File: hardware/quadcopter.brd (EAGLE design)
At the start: 132 x 132 mm, 69 parts, among them J2 AVR_SPI_PRG_6-SMD, J3 HEADER-10POSTH-254X10, J4 HEADER-4POS-0.1IN-FEMALE-SMD-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, J6 HEADER-4POS-0.1IN-FEMALE, Q3 MOSFET-FET-SI2302CDS-T1-E3CT-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, Q4 MOSFET-FET-SI2302CDS-T1-E3CT-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, Q5 MOSFET-FET-SI2302CDS-T1-E3CT-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, Q6 MOSFET-FET-SI2302CDS-T1-E3CT-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, U1 ATMEGA128RFA1, U2 IMU-LSM6DSOXTR-497-18367-1-ND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

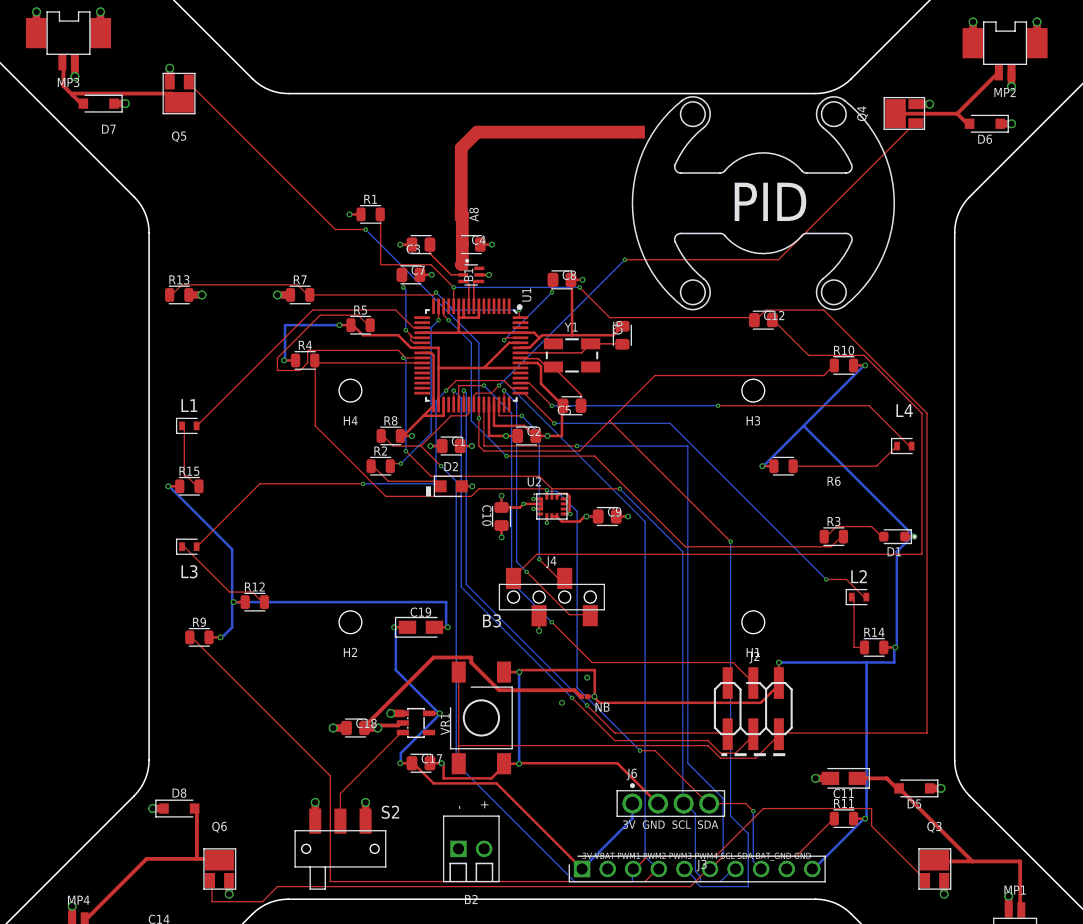
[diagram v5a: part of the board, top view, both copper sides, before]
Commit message: fixed high-current net issues
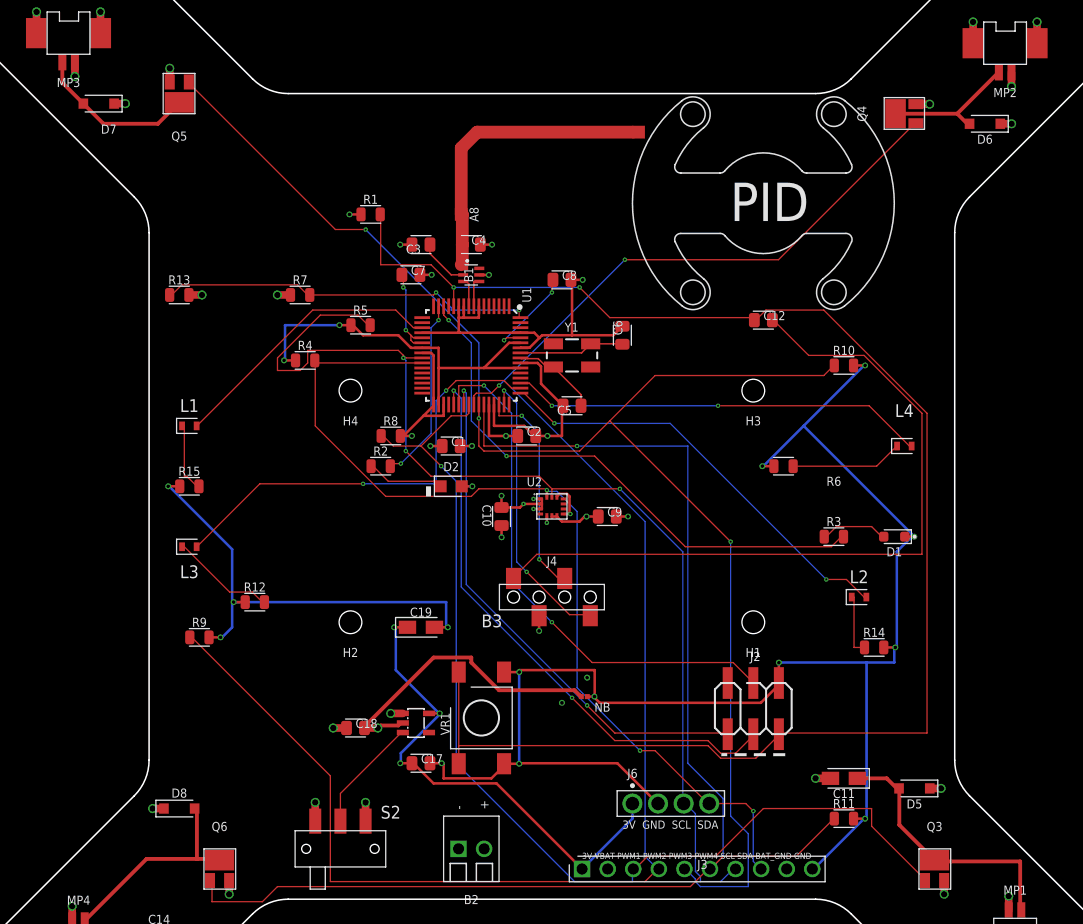
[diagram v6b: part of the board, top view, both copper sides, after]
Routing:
- net N$18: track 28.4 -> 26.7 mm
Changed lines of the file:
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@@
 <class number="1" name="HIGH-I" width="0.381" drill="0">
 </class>
-<class number="3" name="POWER" width="0" drill="0">
+<class number="3" name="PWR" width="0.254" drill="0">
 </class>
 <class number="4" name="RFSIG" width="0" drill="0">
@@
 </via>
 </signal>
-<signal name="N$18">
+<signal name="N$18" class="1">
 <contactref element="Q3" pad="D"/>
 <contactref element="MP1" pad="2"/>
@@
 <wire x1="34.25" y1="-28" x2="34.475" y2="-28" width="0.381" layer="1"/>
 <wire x1="46.5" y1="-35.25" x2="46.5" y2="-40" width="0.381" layer="1"/>
-<wire x1="38" y1="-35.25" x2="41.75" y2="-35.25" width="0.381" layer="1"/>
-<wire x1="41.75" y1="-35.25" x2="46.5" y2="-35.25" width="0.381" layer="1"/>
+<wire x1="38" y1="-35.25" x2="46.5" y2="-35.25" width="0.381" layer="1"/>
 <wire x1="46.5" y1="-40" x2="46.6125" y2="-40.1" width="0.381" layer="1"/>
 <wire x1="38" y1="-35.25" x2="38" y2="-35.125" width="0.381" layer="1"/>
-<wire x1="41.75" y1="-35.25" x2="34.5" y2="-28" width="0.381" layer="1"/>
 <wire x1="34.5" y1="-28" x2="34.475" y2="-28" width="0.381" layer="1"/>
-</signal>
-<signal name="N$19">
+<wire x1="38" y1="-35.125" x2="34.5" y2="-31.625" width="0.381" layer="1"/>
+<wire x1="34.5" y1="-31.625" x2="34.5" y2="-28" width="0.381" layer="1"/>
+</signal>
+<signal name="N$19" class="1">
 <contactref element="Q4" pad="D"/>
 <contactref element="MP2" pad="2"/>
@@
 <wire x1="44.25" y1="43" x2="44.3875" y2="43.1" width="0.381" layer="1"/>
 </signal>
-<signal name="N$20">
+<signal name="N$20" class="1">
 <contactref element="Q5" pad="D"/>
 <contactref element="MP3" pad="2"/>
 <contactref element="D7" pad="2"/>
-<wire x1="-48.5" y1="41.75" x2="-47.625" y2="40.875" width="0.381" layer="1"/>
-<wire x1="-47.625" y1="40.875" x2="-46.75" y2="40" width="0.381" layer="1"/>
-<wire x1="-48.5" y1="44" x2="-48.5" y2="41.75" width="0.381" layer="1"/>
-<wire x1="-46.75" y1="40" x2="-46.525" y2="40" width="0.381" layer="1"/>
-<wire x1="-48.5" y1="44" x2="-48.6125" y2="44.1" width="0.381" layer="1"/>
-<wire x1="-37.75" y1="41" x2="-37" y2="40.25" width="0.381" layer="1"/>
-<wire x1="-47.5" y1="41" x2="-37.75" y2="41" width="0.381" layer="1"/>
-<wire x1="-37" y1="40.25" x2="-37" y2="40.125" width="0.381" layer="1"/>
-<wire x1="-47.5" y1="41" x2="-47.625" y2="40.875" width="0.381" layer="1"/>
-</signal>
-<signal name="N$21">
+<wire x1="-48.6125" y1="44.1" x2="-48.6125" y2="42.0875" width="0.381" layer="1"/>
+<wire x1="-48.6125" y1="42.0875" x2="-46.525" y2="40" width="0.381" layer="1"/>
+<wire x1="-37" y1="40.125" x2="-39.125" y2="38" width="0.381" layer="1"/>
+<wire x1="-39.125" y1="38" x2="-44.525" y2="38" width="0.381" layer="1"/>
+<wire x1="-44.525" y1="38" x2="-46.525" y2="40" width="0.381" layer="1"/>
+</signal>
+<signal name="N$21" class="1">
 <contactref element="Q6" pad="D"/>
 <contactref element="MP4" pad="2"/>

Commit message: i really hope this passes
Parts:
- moved LOGO 58.8 mm to (12.0, -19.1)
- moved J6 26.6 mm to (-1.00, -4.50), turned to 0.9 degrees
- moved D7 25.5 mm to (-34.0, 17.0)
- moved MP3 21.2 mm to (-33.0, 32.0)
- moved C14 20.8 mm to (-27.0, -25.5)
- moved MP4 19.8 mm to (-33.0, -30.0)
- moved J2 19.3 mm to (19.9, -0.77)
- moved Q5 18.4 mm to (-33.0, 23.0)
- moved D6 18.0 mm to (28.0, 28.0), turned to 0 degrees
- moved MP1 17.8 mm to (35.0, -29.0)
- moved Q6 17.1 mm to (-27.0, -20.0)
- moved MP2 16.6 mm to (35.3, 32.5)
- moved Q3 16.1 mm to (36.0, -20.0)
- moved D5 14.0 mm to (36.0, -14.0)
- moved Q4 14.0 mm to (35.0, 25.0)
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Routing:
- net GND: track 291.8 -> 66.3 mm, vias 29 -> 28
- net SCL: track 108.5 -> 75.0 mm, vias 3 -> 2
- net N$13: track 74.3 -> 42.8 mm, vias 0 -> 2
- net PWM2: track 174.2 -> 146.1 mm, vias 2 -> 1
- net RESET: track 157.8 -> 133.8 mm, vias 2 -> 4
- net PWM4: track 135.8 -> 112.2 mm, vias 1 -> 2
- net MISO: track 52.8 -> 32.6 mm
- net MOSI: track 53.2 -> 36.1 mm
- net SCK: track 57.9 -> 43.3 mm
- net PWM3: track 149.4 -> 135.9 mm
- net SDA: track 94.5 -> 82.3 mm, vias 3 -> 2
- net BATMEASURE: track 37.4 -> 45.8 mm
- net PWM1: track 103.5 -> 96.1 mm
- net N$21: track 21.3 -> 14.8 mm
- net 3V: track 105.0 -> 98.9 mm, vias 12 -> 13
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- added copper zone on layer 1, net GND
- added copper zone on layer 16, net GND
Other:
- outline, holes or cut-outs redrawn

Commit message: i really hope this one passes
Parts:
- moved R4 17.7 mm to (-15.5, -0.70)
- moved C18 5.92 mm to (-14.6, -25.0)
- moved C19 5.74 mm to (-15.2, -17.3)
- moved C7 4.60 mm to (-18.6, 23.0)
- moved C3 2.94 mm to (-12.5, 23.1)
- moved C17 2.89 mm to (-16.0, -29.8)
- moved B3 1.66 mm to (-8.50, -21.0)
- moved C9 1.41 mm to (6.50, 0.00)
- moved R7 0.92 mm to (-25.7, 21.6)
- moved Q4 0.80 mm to (35.0, 24.2)
- moved C11 0.20 mm to (29.1, -20.0)
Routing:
- net PWM2: track 146.1 -> 159.9 mm, vias 1 -> 3
- net SCL: track 75.0 -> 85.4 mm, vias 2 -> 1
- net PWM3: track 135.9 -> 129.7 mm
- net 3V: track 98.9 -> 92.8 mm
- net SCK: track 43.3 -> 38.2 mm
- net PG0: track 54.4 -> 49.7 mm
- net SDA: track 82.3 -> 85.1 mm
- net N$13: track 42.8 -> 40.1 mm
- net MOSI: track 36.1 -> 33.7 mm
- net RESET: track 133.8 -> 131.6 mm, vias 4 -> 3
- net N$5: track 5.07 -> 2.84 mm
- net LED2: track 42.7 -> 44.9 mm, vias 2 -> 0
- net N$9: track 9.80 -> 11.8 mm
- net LED3: track 41.7 -> 43.2 mm
- net PWM1: track 96.1 -> 97.6 mm
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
